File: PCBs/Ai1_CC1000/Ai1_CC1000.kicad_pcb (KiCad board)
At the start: 4 copper layers, 68.8 x 41.9 mm, 49 parts, among them J1 MCU_Cons, J2 MCU_D, J3 MCU_A, J4 RF_Control, U1 CC1000, U10 ADG918BRM, U11 ADG918BRM, U2 ADG918BRM, U3 ADG918BRM, U4 ADG918BRM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

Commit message: Layout V2
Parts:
- removed U10, U11, U2, U3, U4, U5, U6, U7, U8, U9: ADG918BRM, Package_SO:MSOP-8_3x3mm_P0.65mm
- added IC1: BGS12WN6E6329XTSA1, Package_LGA:Infineon_PG-TSNP-6-10_0.7x1.1mm_0.7x1.1mm_P0.4mm, F.Cu at (118.7, 66.6)
- added IC10: BGS12WN6E6329XTSA1, Package_LGA:Infineon_PG-TSNP-6-10_0.7x1.1mm_0.7x1.1mm_P0.4mm, F.Cu at (115.8, 106.0)
- added IC2: BGS12WN6E6329XTSA1, Package_LGA:Infineon_PG-TSNP-6-10_0.7x1.1mm_0.7x1.1mm_P0.4mm, F.Cu at (120.6, 66.2)
- added IC3: BGS12WN6E6329XTSA1, Package_LGA:Infineon_PG-TSNP-6-10_0.7x1.1mm_0.7x1.1mm_P0.4mm, F.Cu at (118.7, 68.6)
- added IC4: BGS12WN6E6329XTSA1, Package_LGA:Infineon_PG-TSNP-6-10_0.7x1.1mm_0.7x1.1mm_P0.4mm, F.Cu at (120.6, 68.4)
- added IC5: BGS12WN6E6329XTSA1, Package_LGA:Infineon_PG-TSNP-6-10_0.7x1.1mm_0.7x1.1mm_P0.4mm, F.Cu at (98.2, 70.4)
- added IC6: BGS12WN6E6329XTSA1, Package_LGA:Infineon_PG-TSNP-6-10_0.7x1.1mm_0.7x1.1mm_P0.4mm, F.Cu at (99.7, 70.0)
- added IC7: BGS12WN6E6329XTSA1, Package_LGA:Infineon_PG-TSNP-6-10_0.7x1.1mm_0.7x1.1mm_P0.4mm, F.Cu at (109.0, 106.3)
- added IC8: BGS12WN6E6329XTSA1, Package_LGA:Infineon_PG-TSNP-6-10_0.7x1.1mm_0.7x1.1mm_P0.4mm, F.Cu at (110.5, 105.9)
- added IC9: BGS12WN6E6329XTSA1, Package_LGA:Infineon_PG-TSNP-6-10_0.7x1.1mm_0.7x1.1mm_P0.4mm, F.Cu at (114.3, 106.4)
- C31_0, C41_0, C42_0, L32_0, L41_0: moved to B.Cu
- L101_0, L101_1, L101_2: moved to F.Cu
- moved L101_2 34.7 mm to (106.8, 100.5)
- moved L101_0 31.6 mm to (106.8, 94.5), turned to 0 degrees
- moved L101_1 31.4 mm to (106.8, 97.5)
- moved C31_0 13.3 mm to (119.3, 67.5), turned to 0 degrees
- moved C42_2 12.7 mm to (116.1, 68.8)
- moved L41_2 11.5 mm to (115.9, 70.6), turned to 180 degrees
- moved C31_1 9.37 mm to (115.9, 63.4), turned to 0 degrees
- moved C42_0 9.20 mm to (119.4, 69.9)
- moved L32_0 8.77 mm to (119.2, 65.6)
- moved C31_2 8.42 mm to (115.9, 65.0), turned to 0 degrees
- moved L32_1 7.97 mm to (115.8, 61.5)
- moved C42_1 6.07 mm to (115.8, 72.6), turned to 0 degrees
- moved L32_2 4.29 mm to (115.8, 66.9), turned to 180 degrees
- moved C41_1 3.87 mm to (115.8, 74.2), turned to 0 degrees
- moved C41_0 3.57 mm to (119.3, 73.5), turned to 0 degrees
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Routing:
- net /433Mhz_Out: track 0.00 -> 10.4 mm
- net /To_Ant_433Mhz: track 0.00 -> 10.3 mm
- net VDDA: track 0.00 -> 6.24 mm, vias 0 -> 9
- net /433MHz_In: track 0.00 -> 5.69 mm
- net /315Mhz_Out: track 0.00 -> 4.97 mm, vias 0 -> 1
- net /915Mhz_Out: track 0.00 -> 4.28 mm
- net /To_Ant_915Mhz: track 0.00 -> 4.01 mm
- net /315MHz_In: track 0.00 -> 4.01 mm, vias 0 -> 1
- net /915MHz_In: track 0.00 -> 3.92 mm
- net Net-(IC3-RFIN): track 0.00 -> 3.43 mm
- net GNDA: track 0.00 -> 2.89 mm, vias 0 -> 20
- net /To_Ant_315Mhz: track 0.00 -> 2.48 mm
- net /OUT_Matching: track 0.00 -> 2.37 mm
- net /IN_Matching: track 0.00 -> 2.26 mm
- net Net-(IC1-RFIN): track 0.00 -> 1.56 mm
- added copper zone on In1.Cu, net GNDA
- added copper zone on In2.Cu, net VDDA

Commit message: Layout V3 Antena needs attention
To check with prof
Antenas? Multiple?
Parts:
- added J10: RF_S_C, Connector_PinSocket_2.54mm:PinSocket_1x01_P2.54mm_Vertical, F.Cu at (121.6, 83.3)
- added J11: RF_S_C, Connector_PinSocket_2.54mm:PinSocket_1x01_P2.54mm_Vertical, F.Cu at (124.1, 83.3)
- added J12: RF_S_C, Connector_PinSocket_2.54mm:PinSocket_1x01_P2.54mm_Vertical, F.Cu at (129.2, 83.3)
- added J13: RF_S_C, Connector_PinSocket_2.54mm:PinSocket_1x01_P2.54mm_Vertical, F.Cu at (126.6, 83.3)
- added J5: RF_S_C, Connector_PinSocket_2.54mm:PinSocket_1x01_P2.54mm_Vertical, F.Cu at (116.0, 56.4)
- added J6: RF_S_C, Connector_PinSocket_2.54mm:PinSocket_1x01_P2.54mm_Vertical, F.Cu at (121.0, 56.4)
- added J7: RF_S_C, Connector_PinSocket_2.54mm:PinSocket_1x01_P2.54mm_Vertical, F.Cu at (113.4, 56.4)
- added J8: RF_S_C, Connector_PinSocket_2.54mm:PinSocket_1x01_P2.54mm_Vertical, F.Cu at (110.9, 56.4)
- added J9: RF_S_C, Connector_PinSocket_2.54mm:PinSocket_1x01_P2.54mm_Vertical, F.Cu at (108.3, 56.4)
- J4: value RF_Control -> RF_S_C; footprint Connector_PinSocket_2.54mm:PinSocket_2x05_P2.54mm_Vertical -> Connector_PinSocket_2.54mm:PinSocket_1x01_P2.54mm_Vertical
- moved IC10 31.4 mm to (128.2, 77.2)
- moved IC8 31.2 mm to (122.6, 77.2), turned to 180 degrees
- moved IC9 30.8 mm to (128.2, 79.0)
- moved IC7 30.5 mm to (122.6, 79.0), turned to 180 degrees
- moved L101_2 29.1 mm to (125.4, 78.2)
- moved L101_0 26.1 mm to (125.4, 76.1)
- moved L101_1 25.4 mm to (125.4, 80.2)
- moved J4 18.0 mm to (118.5, 56.4), turned to 0 degrees
- moved AE1 14.9 mm to (108.1, 67.9)
- moved IC5 14.4 mm to (112.2, 67.1)
- moved IC6 12.6 mm to (112.3, 69.8)
- moved C42_1 5.41 mm to (115.3, 67.3)
- moved C41_1 5.38 mm to (115.3, 68.8)
- moved L41_1 5.34 mm to (115.1, 70.6)
- moved C41_0 4.47 mm to (119.4, 69.0)
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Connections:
- IC4 pad 1: /315Mhz_Out -> Net-(IC3-RFIN)
- IC4 pad 3: Net-(IC3-RFIN) -> /315Mhz_Out
- IC8 pad 1: /L_315_1 -> Net-(IC7-RFIN)
- IC8 pad 3: Net-(IC7-RFIN) -> /L_315_1
- IC9 pad 1: /L_433_2 -> /L_915_2
- IC9 pad 3: /L_915_2 -> /L_433_2
- J1 pad 1: Net-(J1-Pin_1) -> /PALE
- J1 pad 2: Net-(J1-Pin_2) -> /PDATA
- J1 pad 3: Net-(J1-Pin_3) -> /PCLK
- J1 pad 4: Net-(J1-Pin_4) -> /DCLK
- J1 pad 5: Net-(J1-Pin_5) -> /DIO
- U1 pad 23: Net-(J1-Pin_2) -> /DIO
- U1 pad 24: Net-(J1-Pin_1) -> /DCLK
- U1 pad 25: Net-(J1-Pin_4) -> /PCLK
- U1 pad 26: Net-(J1-Pin_5) -> /PDATA
- U1 pad 27: Net-(J1-Pin_3) -> /PALE
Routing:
- net GNDD: track 0.00 -> 41.1 mm
- net VDD: track 0.00 -> 31.5 mm
- net Net-(J2-Pin_1): track 0.00 -> 31.5 mm, vias 0 -> 1
- net /DIO: track 0.00 -> 21.5 mm, vias 0 -> 1
- net /DCLK: track 0.00 -> 18.7 mm, vias 0 -> 1
- net /PCLK: track 0.00 -> 15.8 mm, vias 0 -> 1
- net /C_RFS_4: track 0.00 -> 14.3 mm, vias 0 -> 1
- net /OSC2: track 0.00 -> 14.2 mm
- net /PDATA: track 0.00 -> 13.7 mm, vias 0 -> 1
- net Net-(J3-Pin_1): track 0.00 -> 12.8 mm, vias 0 -> 1
- net /OSC1: track 0.00 -> 12.5 mm
- net /C_RFS_3: track 0.00 -> 12.3 mm, vias 0 -> 1
- net /PALE: track 0.00 -> 12.0 mm, vias 0 -> 1
- net /C_RFS_2: track 0.00 -> 11.2 mm, vias 0 -> 1
- net /C_RFS_1: track 0.00 -> 10.9 mm, vias 0 -> 1
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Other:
- board size 68.8 x 41.9 mm -> 48.4 x 41.9 mm

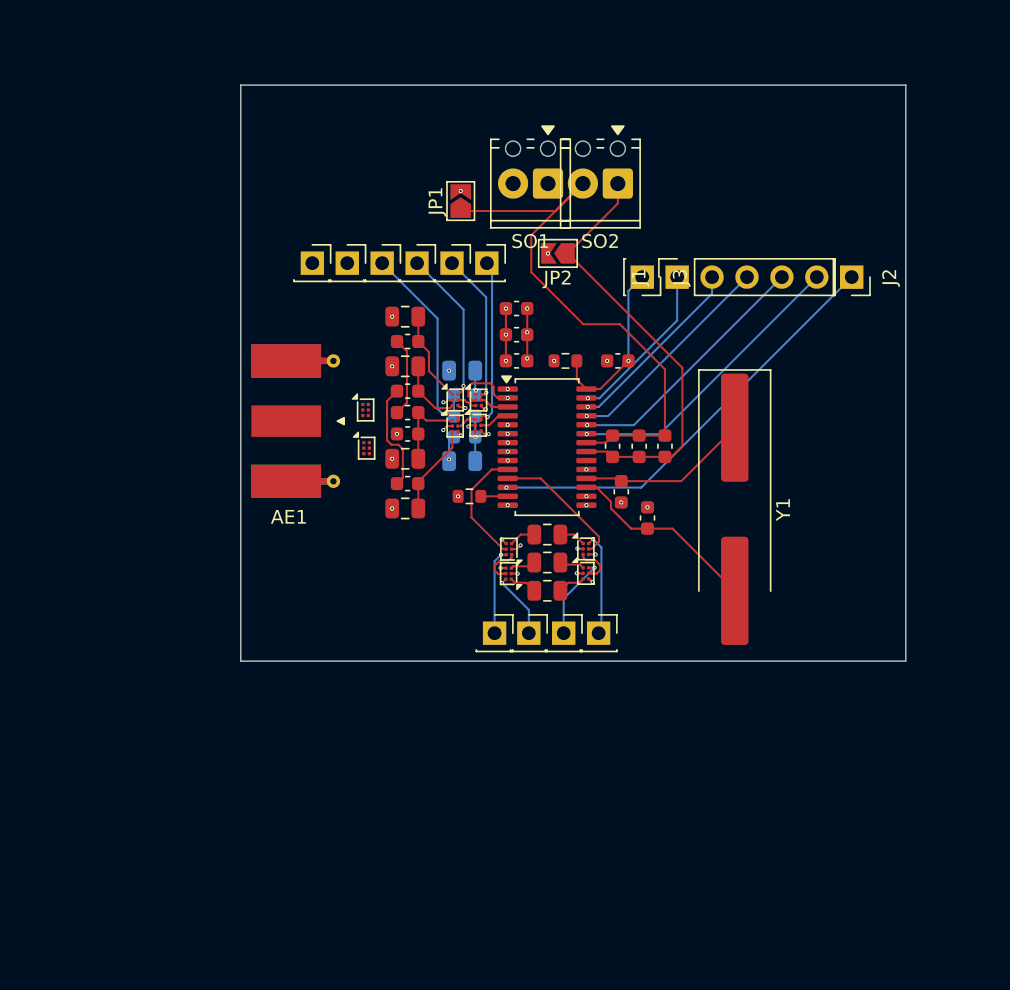
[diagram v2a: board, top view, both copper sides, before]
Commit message: PCB ready for fab 1 ?
Problemas atuais, antena e uma revisao sobre os traces, mas de acordo com a calculador de microstrip nenhum trace tem mais q 15EL ou seja menos de /4 entao nao devem desviar o matching
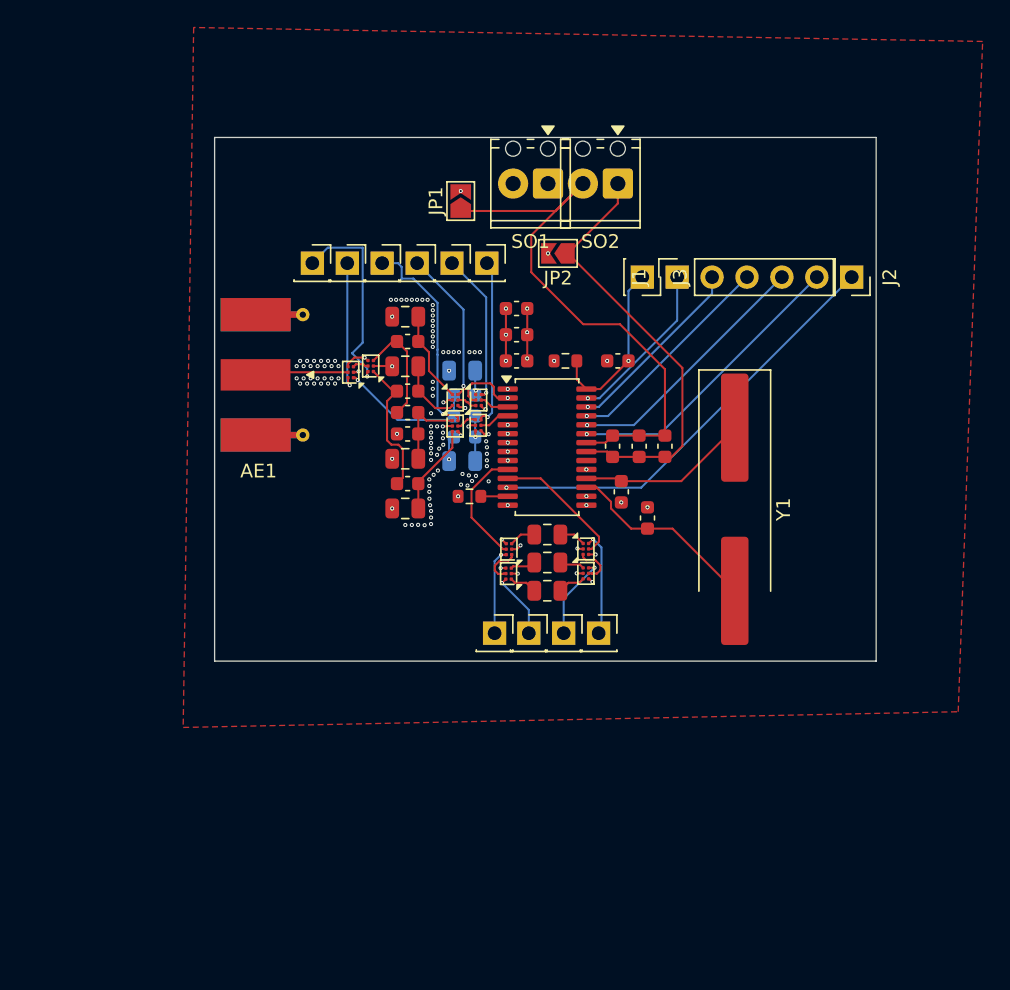
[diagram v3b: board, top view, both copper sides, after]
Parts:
- moved IC6 5.64 mm to (111.1, 64.3), turned to 180 degrees
- moved AE1 4.04 mm to (105.9, 64.5)
- moved IC5 3.22 mm to (112.6, 63.9), turned to 180 degrees
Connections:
- IC5 pad 1: /To_Ant_433Mhz -> /To_Ant_915Mhz
- IC5 pad 3: /To_Ant_915Mhz -> /To_Ant_433Mhz
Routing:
- net /C_RFS_6: track 0.00 -> 14.7 mm, vias 0 -> 1
- net /C_RFS_5: track 0.00 -> 9.55 mm, vias 0 -> 1
- net /To_Ant_315Mhz: track 1.52 -> 10.2 mm, vias 0 -> 1
- net /To_Ant: track 0.00 -> 6.80 mm
- net /To_Ant_915Mhz: track 7.98 -> 10.3 mm
- net /To_Ant_433Mhz: track 5.77 -> 8.06 mm
- net VDDA: track 9.60 -> 11.5 mm, vias 20 -> 33
- net GNDA: track 13.0 -> 14.7 mm, vias 26 -> 108
- net Net-(IC5-RFIN): track 0.00 -> 1.18 mm
- net /C_RFS_4: track 14.3 -> 15.5 mm
- added copper zone on F.Cu, net GNDA
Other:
- board size 48.4 x 41.9 mm -> 48.1 x 38.1 mm

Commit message: gerbers
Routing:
- net VDDA: vias 33 -> 26
- net GNDA: vias 108 -> 386
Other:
- board size 48.1 x 38.1 mm -> 47.8 x 39.5 mm
